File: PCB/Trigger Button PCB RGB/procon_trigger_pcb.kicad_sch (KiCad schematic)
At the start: 10 parts, among them J1 Conn_01x05_Pin, J2 Conn_01x05_Pin, SW1 SW_Push, SW2 SW_Push, SW3 SW_Push, SW4 SW_Push

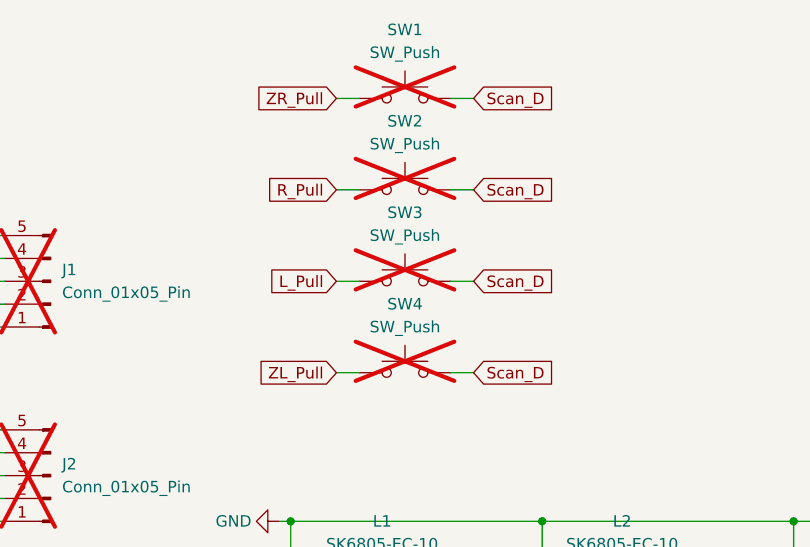
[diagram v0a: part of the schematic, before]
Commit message: Added switch to trigger board
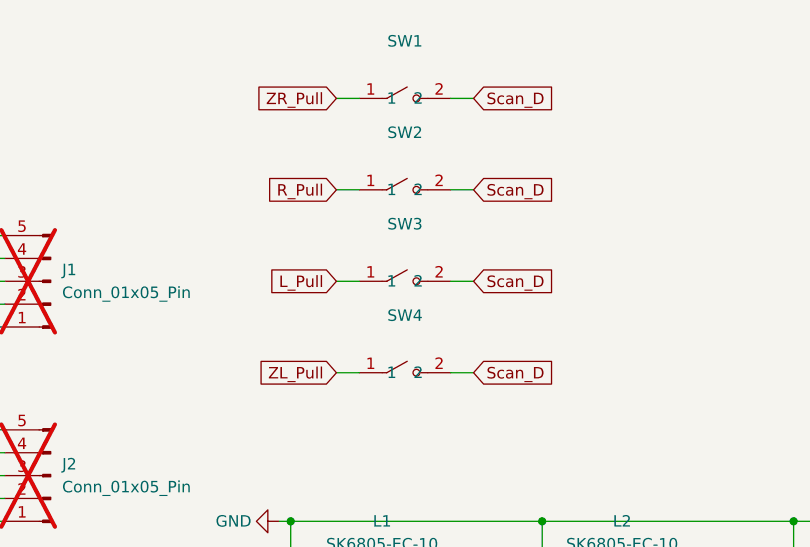
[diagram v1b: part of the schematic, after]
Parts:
- SW1, SW2, SW3, SW4: footprint hhl:starprint -> hhl:SW-SMD_L6.0-W3.5-LS8.0_TS04-TBW1FH4.3; symbol Switch:SW_Push -> hhl:TS04-TBW1FH4.3; LCSC Part (none) -> C22362989; now fitted
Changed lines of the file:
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@@
 (kicad_sch
-	(version 20231120)
+	(version 20250114)
 	(generator "eeschema")
-	(generator_version "8.0")
+	(generator_version "9.0")
 	(paper "A4")
 	(title_block
@@
 		(on_board yes)
 		(dnp no)
-		(property "Reference" "#PWR04"
+		(property "Reference" "#PWR03"
 			(at 107.95 113.03 0)
 			(effects
@@
 			)
 		)
-		(property "Description" ""
+		(property "Description" "Power symbol creates a global label with name \"GND\" , ground"
 			(at 114.3 113.03 0)
 			(effects
@@
 			)
 		)
-		(property "Description" "-"
+		(property "Description" "Generic connector, single row, 01x05, script generated"
 			(at 88.9 107.95 0)
 			(effects
@@
 	)
 	(symbol
-		(lib_id "Switch:SW_Push")
+		(lib_id "hhl:TS04-TBW1FH4.3")
 		(at 128.27 86.36 0)
 		(unit 1)
@@
 		(in_bom yes)
 		(on_board yes)
-		(dnp yes)
+		(dnp no)
 		(fields_autoplaced yes)
 		(property "Reference" "SW3"
-			(at 128.27 78.74 0)
+			(at 128.27 80.01 0)
 			(effects
 				(font
@@
 		)
 		(property "Value" "SW_Push"
-			(at 128.27 81.28 0)
-			(effects
-				(font
-					(size 1.27 1.27)
-				)
-			)
-		)
-		(property "Footprint" "hhl:starprint"
-			(at 128.27 81.28 0)
+			(at 128.27 82.55 0)
+			(effects
+				(font
+					(size 1.27 1.27)
+				)
+				(hide yes)
+			)
+		)
+		(property "Footprint" "hhl:SW-SMD_L6.0-W3.5-LS8.0_TS04-TBW1FH4.3"
+			(at 128.27 93.98 0)
 			(effects
 				(font
@@
 		)
 		(property "Datasheet" "~"
-			(at 128.27 81.28 0)
-			(effects
-				(font
-					(size 1.27 1.27)
-				)
-				(hide yes)
-			)
-		)
-		(property "Description" ""
+			(at 128.27 86.36 0)
+			(effects
+				(font
+					(size 1.27 1.27)
+				)
+				(hide yes)
+			)
+		)
+		(property "Description" "Push button switch, generic, two pins"
 			(at 128.27 86.36 0)
 			(effects
@@
 		(property "Package" ""
 			(at 128.27 86.36 0)
+			(effects
+				(font
+					(size 1.27 1.27)
+				)
+				(hide yes)
+			)
+		)
+		(property "LCSC Part" "C22362989"
+			(at 128.27 96.52 0)
 			(effects
 				(font
@@
 		(on_board yes)
 		(dnp no)
-		(property "Reference" "#PWR04"
+		(property "Reference" "#PWR01"
 			(at 74.93 109.22 0)
 			(effects
@@
 			)
 		)
-		(property "Description" ""
+		(property "Description" "Power symbol creates a global label with name \"GND\" , ground"
 			(at 81.28 109.22 0)
 			(effects
@@
 			)
 		)
-		(property "Description" "-"
+		(property "Description" "Generic connector, single row, 01x05, script generated"
 			(at 88.9 86.36 0)
 			(effects
@@
 		(on_board yes)
 		(dnp no)
-		(property "Reference" "#PWR011"
+		(property "Reference" "#PWR04"
 			(at 135.89 133.35 0)
 			(effects
@@
 			)
 		)
-		(property "Description" ""
+		(property "Description" "Power symbol creates a global label with name \"+3V3\""
 			(at 132.08 133.35 0)
 			(effects
@@
 	)
 	(symbol
-		(lib_id "Switch:SW_Push")
+		(lib_id "hhl:TS04-TBW1FH4.3")
 		(at 128.27 66.04 0)
 		(unit 1)
@@
 		(in_bom yes)
 		(on_board yes)
-		(dnp yes)
+		(dnp no)
 		(fields_autoplaced yes)
 		(property "Reference" "SW1"
-			(at 128.27 58.42 0)
+			(at 128.27 59.69 0)
 			(effects
 				(font
@@
 		)
 		(property "Value" "SW_Push"
-			(at 128.27 60.96 0)
-			(effects
-				(font
-					(size 1.27 1.27)
-				)
-			)
-		)
-		(property "Footprint" "hhl:starprint"
-			(at 128.27 60.96 0)
+			(at 128.27 62.23 0)
+			(effects
+				(font
+					(size 1.27 1.27)
+				)
+				(hide yes)
+			)
+		)
+		(property "Footprint" "hhl:SW-SMD_L6.0-W3.5-LS8.0_TS04-TBW1FH4.3"
+			(at 128.27 73.66 0)
 			(effects
 				(font
@@
 		)
 		(property "Datasheet" "~"
-			(at 128.27 60.96 0)
-			(effects
-				(font
-					(size 1.27 1.27)
-				)
-				(hide yes)
-			)
-		)
-		(property "Description" ""
+			(at 128.27 66.04 0)
+			(effects
+				(font
+					(size 1.27 1.27)
+				)
+				(hide yes)
+			)
+		)
+		(property "Description" "Push button switch, generic, two pins"
 			(at 128.27 66.04 0)
 			(effects
@@
 		(property "Package" ""
 			(at 128.27 66.04 0)
+			(effects
+				(font
+					(size 1.27 1.27)
+				)
+				(hide yes)
+			)
+		)
+		(property "LCSC Part" "C22362989"
+			(at 128.27 76.2 0)
 			(effects
 				(font
@@
 	)
 	(symbol
-		(lib_id "Switch:SW_Push")
+		(lib_id "hhl:TS04-TBW1FH4.3")
 		(at 128.27 76.2 0)
 		(unit 1)
@@
 		(in_bom yes)
 		(on_board yes)
-		(dnp yes)
+		(dnp no)
 		(fields_autoplaced yes)
 		(property "Reference" "SW2"
-			(at 128.27 68.58 0)
+			(at 128.27 69.85 0)
 			(effects
 				(font
@@
 		)
 		(property "Value" "SW_Push"
-			(at 128.27 71.12 0)
-			(effects
-				(font
-					(size 1.27 1.27)
-				)
-			)
-		)
-		(property "Footprint" "hhl:starprint"
-			(at 128.27 71.12 0)
+			(at 128.27 72.39 0)
+			(effects
+				(font
+					(size 1.27 1.27)
+				)
+				(hide yes)
+			)
+		)
+		(property "Footprint" "hhl:SW-SMD_L6.0-W3.5-LS8.0_TS04-TBW1FH4.3"
+			(at 128.27 83.82 0)
 			(effects
 				(font
@@
 		)
 		(property "Datasheet" "~"
-			(at 128.27 71.12 0)
-			(effects
-				(font
-					(size 1.27 1.27)
-				)
-				(hide yes)
-			)
-		)
-		(property "Description" ""
+			(at 128.27 76.2 0)
+			(effects
+				(font
+					(size 1.27 1.27)
+				)
+				(hide yes)
+			)
+		)
+		(property "Description" "Push button switch, generic, two pins"
 			(at 128.27 76.2 0)
 			(effects
@@
 		(property "Package" ""
 			(at 128.27 76.2 0)
+			(effects
+				(font
+					(size 1.27 1.27)
+				)
+				(hide yes)
+			)
+		)
+		(property "LCSC Part" "C22362989"
+			(at 128.27 86.36 0)
 			(effects
 				(font
@@
 		(on_board yes)
 		(dnp no)
-		(property "Reference" "#PWR011"
+		(property "Reference" "#PWR02"
 			(at 85.09 104.14 0)
 			(effects
@@
 			)
 		)
-		(property "Description" ""
+		(property "Description" "Power symbol creates a global label with name \"+3V3\""
 			(at 81.28 104.14 0)
 			(effects
@@
 	)
 	(symbol
-		(lib_id "Switch:SW_Push")
+		(lib_id "hhl:TS04-TBW1FH4.3")
 		(at 128.27 96.52 0)
 		(unit 1)
@@
 		(in_bom yes)
 		(on_board yes)
-		(dnp yes)
+		(dnp no)
 		(fields_autoplaced yes)
 		(property "Reference" "SW4"
-			(at 128.27 88.9 0)
+			(at 128.27 90.17 0)
 			(effects
 				(font
@@
 		)
 		(property "Value" "SW_Push"
-			(at 128.27 91.44 0)
-			(effects
-				(font
-					(size 1.27 1.27)
-				)
-			)
-		)
-		(property "Footprint" "hhl:starprint"
-			(at 128.27 91.44 0)
+			(at 128.27 92.71 0)
+			(effects
+				(font
+					(size 1.27 1.27)
+				)
+				(hide yes)
+			)
+		)
+		(property "Footprint" "hhl:SW-SMD_L6.0-W3.5-LS8.0_TS04-TBW1FH4.3"
+			(at 128.27 104.14 0)
 			(effects
 				(font
@@
 		)
 		(property "Datasheet" "~"
-			(at 128.27 91.44 0)
-			(effects
-				(font
-					(size 1.27 1.27)
-				)
-				(hide yes)
-			)
-		)
-		(property "Description" ""
+			(at 128.27 96.52 0)
+			(effects
+				(font
+					(size 1.27 1.27)
+				)
+				(hide yes)
+			)
+		)
+		(property "Description" "Push button switch, generic, two pins"
 			(at 128.27 96.52 0)
 			(effects
@@
 		(property "Package" ""
 			(at 128.27 96.52 0)
+			(effects
+				(font
+					(size 1.27 1.27)
+				)
+				(hide yes)
+			)
+		)
+		(property "LCSC Part" "C22362989"
+			(at 128.27 106.68 0)
 			(effects
 				(font
@@
 		)
 	)
+	(embedded_fonts no)
 )
